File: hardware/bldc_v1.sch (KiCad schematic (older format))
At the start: 0 parts

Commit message: Updaated Driver section
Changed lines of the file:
@@
 LIBS:valves
 LIBS:infineon
+LIBS:bldc_v1-cache
 EELAYER 25 0
 EELAYER END
@@
 $EndDescr
 $Sheet
-S 1850 1450 1500 1400
+S 1800 1500 1750 1700
 U 5AAE8848
 F0 "GateDriver" 60
 F1 "GateDriver.sch" 60
+F2 "PhaseA" I L 1800 2800 60
+F3 "PhaseB" I L 1800 2900 60
+F4 "PhaseC" I L 1800 3000 60
+F5 "GND" I L 1800 3100 60
+F6 "LS_A_GATE" O R 3550 2000 60
+F7 "HS_A_GATE" O R 3550 1900 60
+F8 "LS_B_GATE" O R 3550 2200 60
+F9 "HS_B_GATE" O R 3550 2100 60
+F10 "LS_C_GATE" O R 3550 2400 60
+F11 "HS_C_GATE" O R 3550 2300 60
+F12 "LS_A_TTL_PWM" I L 1800 2150 60
+F13 "HS_A_TTL_PWM" I L 1800 2050 60
+F14 "LS_B_TTL_PWM" I L 1800 2350 60
+F15 "HS_B_TTL_PWM" I L 1800 2250 60
+F16 "LS_C_TTL_PWM" I L 1800 2550 60
+F17 "HS_C_TTL_PWM" I L 1800 2450 60
+F18 "+12V" I L 1800 1600 60
 $EndSheet
 $Sheet
-S 4950 1450 1550 1450
+S 4800 1500 1550 1450
 U 5AAE8860
 F0 "MOSFETS" 60
 F1 "MOSFETS.sch" 60
-F2 "PhaseA" O R 6500 1900 60
-F3 "+V" I L 4950 1550 60
-F4 "PhaseB" O R 6500 2050 60
-F5 "PhaseC" O R 6500 2200 60
-F6 "GND" O L 4950 2800 60
-F7 "HS_A_GATE" I L 4950 1850 60
-F8 "LS_A_GATE" I L 4950 1950 60
-F9 "HS_B_GATE" I L 4950 2050 60
-F10 "LS_B_GATE" I L 4950 2150 60
-F11 "HS_C_GATE" I L 4950 2250 60
-F12 "LS_C_GATE" I L 4950 2350 60
+F2 "PhaseA" O R 6350 1950 60
+F3 "PhaseB" O R 6350 2100 60
+F4 "PhaseC" O R 6350 2250 60
+F5 "GND" O R 6350 2800 60
+F6 "HS_A_GATE" I L 4800 1900 60
+F7 "LS_A_GATE" I L 4800 2000 60
+F8 "HS_B_GATE" I L 4800 2100 60
+F9 "LS_B_GATE" I L 4800 2200 60
+F10 "HS_C_GATE" I L 4800 2300 60
+F11 "LS_C_GATE" I L 4800 2400 60
+F12 "Vbatt" I L 4800 1600 60
 $EndSheet
+Wire Wire Line
+	3550 1900 4800 1900
+Wire Wire Line
+	3550 2000 4800 2000
+Wire Wire Line
+	3550 2100 4800 2100
+Wire Wire Line
+	3550 2200 4800 2200
+Wire Wire Line
+	3550 2300 4800 2300
+Wire Wire Line
+	3550 2400 4800 2400
+Wire Wire Line
+	6350 2800 6550 2800
+Wire Wire Line
+	6550 2800 6550 3450
+Wire Wire Line
+	6550 3450 1600 3450
+Wire Wire Line
+	1600 3450 1600 3100
+Wire Wire Line
+	1600 3100 1800 3100
+Wire Wire Line
+	6350 2250 6650 2250
+Wire Wire Line
+	6650 2250 6650 3550
+Wire Wire Line
+	6650 3550 1500 3550
+Wire Wire Line
+	1500 3550 1500 3000
+Wire Wire Line
+	1500 3000 1800 3000
+Wire Wire Line
+	6350 2100 6750 2100
+Wire Wire Line
+	6750 2100 6750 3650
+Wire Wire Line
+	6750 3650 1400 3650
+Wire Wire Line
+	1400 3650 1400 2900
+Wire Wire Line
+	1400 2900 1800 2900
+Wire Wire Line
+	6350 1950 6850 1950
+Wire Wire Line
+	6850 1950 6850 3750
+Wire Wire Line
+	6850 3750 1300 3750
+Wire Wire Line
+	1300 3750 1300 2800
+Wire Wire Line
+	1300 2800 1800 2800
 $EndSCHEMATC

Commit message: Update gate driver protection
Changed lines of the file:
@@
 LIBS:valves
 LIBS:infineon
-LIBS:bldc_v1-cache
 EELAYER 25 0
 EELAYER END
@@
 F10 "LS_C_GATE" O R 3550 2400 60
 F11 "HS_C_GATE" O R 3550 2300 60
-F12 "LS_A_TTL_PWM" I L 1800 2150 60
-F13 "HS_A_TTL_PWM" I L 1800 2050 60
-F14 "LS_B_TTL_PWM" I L 1800 2350 60
-F15 "HS_B_TTL_PWM" I L 1800 2250 60
-F16 "LS_C_TTL_PWM" I L 1800 2550 60
-F17 "HS_C_TTL_PWM" I L 1800 2450 60
+F12 "LS_A_TTL_PWM" I L 1800 2000 60
+F13 "HS_A_TTL_PWM" I L 1800 1900 60
+F14 "LS_B_TTL_PWM" I L 1800 2200 60
+F15 "HS_B_TTL_PWM" I L 1800 2100 60
+F16 "LS_C_TTL_PWM" I L 1800 2400 60
+F17 "HS_C_TTL_PWM" I L 1800 2300 60
 F18 "+12V" I L 1800 1600 60
 $EndSheet
 $Sheet
-S 4800 1500 1550 1450
+S 4800 1500 1500 1750
 U 5AAE8860
 F0 "MOSFETS" 60
 F1 "MOSFETS.sch" 60
-F2 "PhaseA" O R 6350 1950 60
-F3 "PhaseB" O R 6350 2100 60
-F4 "PhaseC" O R 6350 2250 60
-F5 "GND" O R 6350 2800 60
+F2 "PhaseA" O R 6300 1950 60
+F3 "PhaseB" O R 6300 2100 60
+F4 "PhaseC" O R 6300 2250 60
+F5 "GND" O R 6300 2800 60
 F6 "HS_A_GATE" I L 4800 1900 60
 F7 "LS_A_GATE" I L 4800 2000 60
@@
 F11 "LS_C_GATE" I L 4800 2400 60
 F12 "Vbatt" I L 4800 1600 60
+F13 "+5V" I L 4800 1700 60
+F14 "FB_A" O R 6300 1600 60
+F15 "FB_B" O R 6300 1700 60
 $EndSheet
 Wire Wire Line
@@
 	3550 2400 4800 2400
 Wire Wire Line
-	6350 2800 6550 2800
+	6300 2800 6550 2800
 Wire Wire Line
 	6550 2800 6550 3450
@@
 	1600 3100 1800 3100
 Wire Wire Line
-	6350 2250 6650 2250
+	6300 2250 6650 2250
 Wire Wire Line
 	6650 2250 6650 3550
@@
 	1500 3000 1800 3000
 Wire Wire Line
-	6350 2100 6750 2100
+	6300 2100 6750 2100
 Wire Wire Line
 	6750 2100 6750 3650
@@
 	1400 2900 1800 2900
 Wire Wire Line
-	6350 1950 6850 1950
+	6300 1950 6850 1950
 Wire Wire Line
 	6850 1950 6850 3750

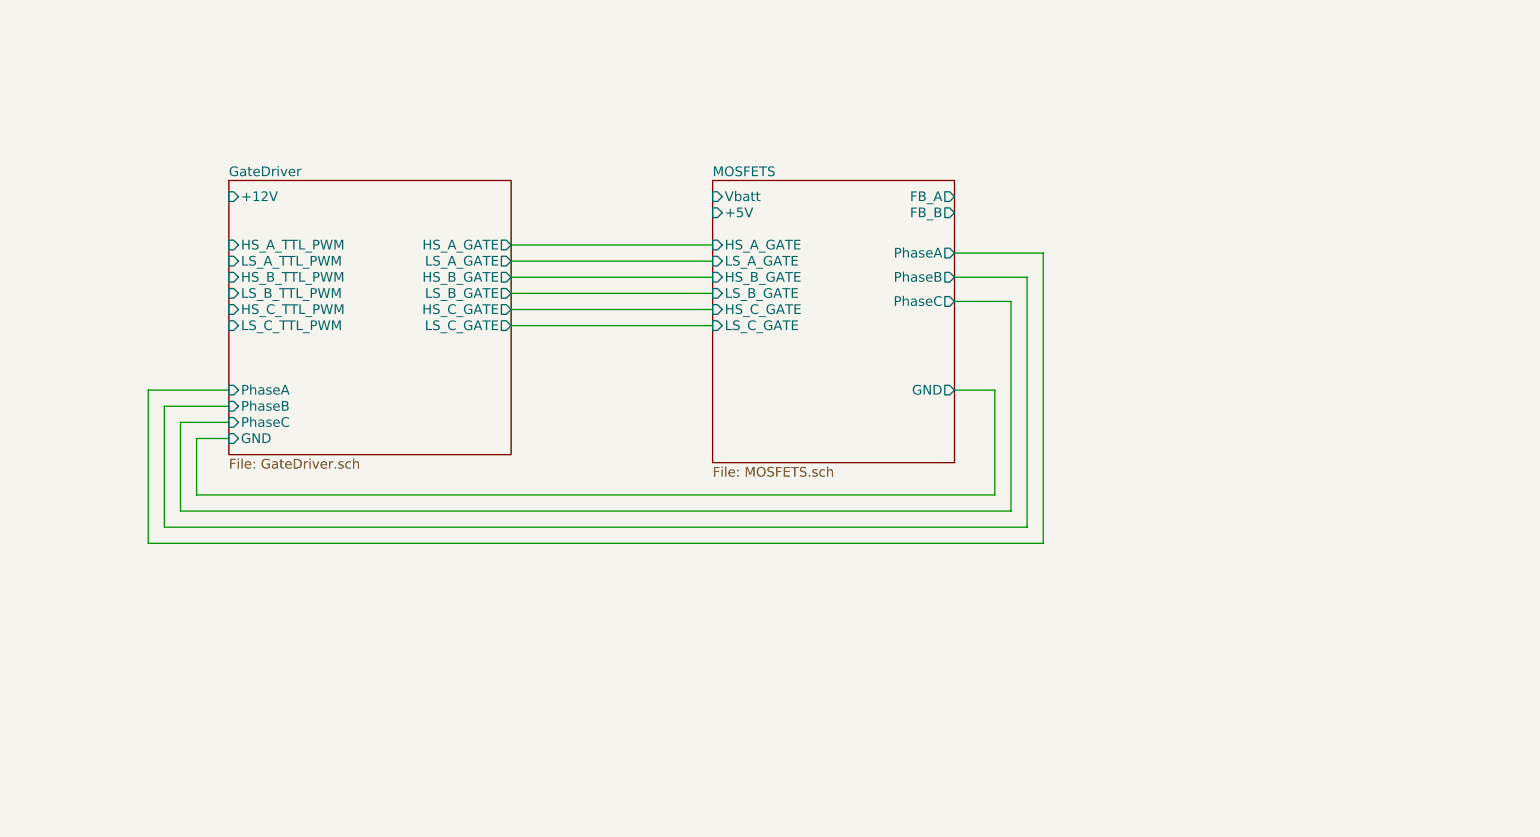
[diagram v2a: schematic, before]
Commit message: Added power converters
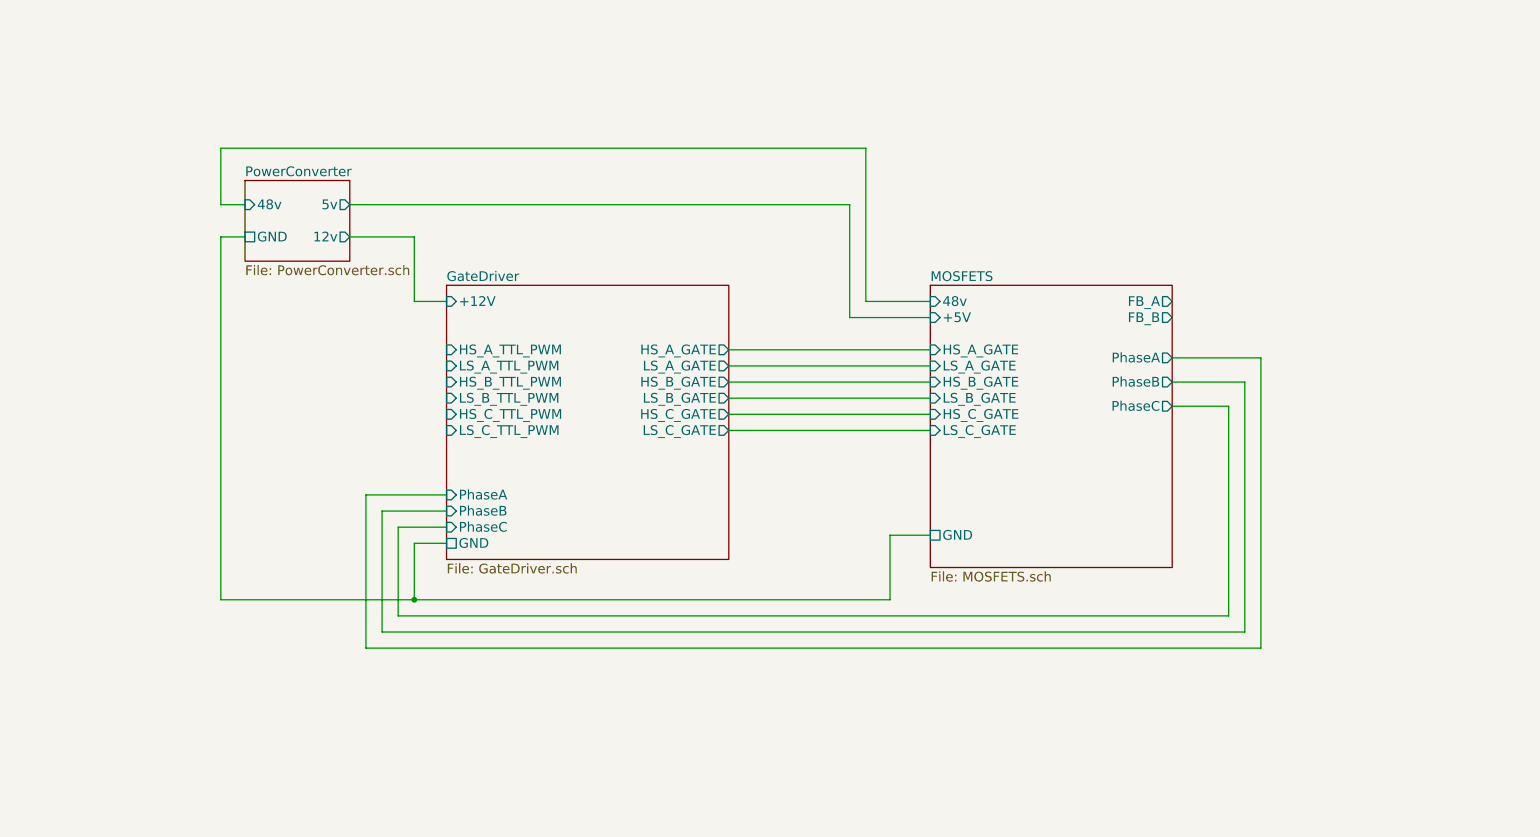
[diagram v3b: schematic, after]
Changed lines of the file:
@@
 $Descr A4 11693 8268
 encoding utf-8
-Sheet 1 3
+Sheet 1 4
 Title "Brushless DC controller"
 Date "2018-03-16"
@@
 $EndDescr
 $Sheet
-S 1800 1500 1750 1700
+S 3150 2150 1750 1700
 U 5AAE8848
 F0 "GateDriver" 60
 F1 "GateDriver.sch" 60
-F2 "PhaseA" I L 1800 2800 60
-F3 "PhaseB" I L 1800 2900 60
-F4 "PhaseC" I L 1800 3000 60
-F5 "GND" I L 1800 3100 60
-F6 "LS_A_GATE" O R 3550 2000 60
-F7 "HS_A_GATE" O R 3550 1900 60
-F8 "LS_B_GATE" O R 3550 2200 60
-F9 "HS_B_GATE" O R 3550 2100 60
-F10 "LS_C_GATE" O R 3550 2400 60
-F11 "HS_C_GATE" O R 3550 2300 60
-F12 "LS_A_TTL_PWM" I L 1800 2000 60
-F13 "HS_A_TTL_PWM" I L 1800 1900 60
-F14 "LS_B_TTL_PWM" I L 1800 2200 60
-F15 "HS_B_TTL_PWM" I L 1800 2100 60
-F16 "LS_C_TTL_PWM" I L 1800 2400 60
-F17 "HS_C_TTL_PWM" I L 1800 2300 60
-F18 "+12V" I L 1800 1600 60
+F2 "PhaseA" I L 3150 3450 60
+F3 "PhaseB" I L 3150 3550 60
+F4 "PhaseC" I L 3150 3650 60
+F5 "GND" U L 3150 3750 60
+F6 "LS_A_GATE" O R 4900 2650 60
+F7 "HS_A_GATE" O R 4900 2550 60
+F8 "LS_B_GATE" O R 4900 2850 60
+F9 "HS_B_GATE" O R 4900 2750 60
+F10 "LS_C_GATE" O R 4900 3050 60
+F11 "HS_C_GATE" O R 4900 2950 60
+F12 "LS_A_TTL_PWM" I L 3150 2650 60
+F13 "HS_A_TTL_PWM" I L 3150 2550 60
+F14 "LS_B_TTL_PWM" I L 3150 2850 60
+F15 "HS_B_TTL_PWM" I L 3150 2750 60
+F16 "LS_C_TTL_PWM" I L 3150 3050 60
+F17 "HS_C_TTL_PWM" I L 3150 2950 60
+F18 "+12V" I L 3150 2250 60
 $EndSheet
 $Sheet
-S 4800 1500 1500 1750
+S 6150 2150 1500 1750
 U 5AAE8860
 F0 "MOSFETS" 60
 F1 "MOSFETS.sch" 60
-F2 "PhaseA" O R 6300 1950 60
-F3 "PhaseB" O R 6300 2100 60
-F4 "PhaseC" O R 6300 2250 60
-F5 "GND" O R 6300 2800 60
-F6 "HS_A_GATE" I L 4800 1900 60
-F7 "LS_A_GATE" I L 4800 2000 60
-F8 "HS_B_GATE" I L 4800 2100 60
-F9 "LS_B_GATE" I L 4800 2200 60
-F10 "HS_C_GATE" I L 4800 2300 60
-F11 "LS_C_GATE" I L 4800 2400 60
-F12 "Vbatt" I L 4800 1600 60
-F13 "+5V" I L 4800 1700 60
-F14 "FB_A" O R 6300 1600 60
-F15 "FB_B" O R 6300 1700 60
+F2 "PhaseA" O R 7650 2600 60
+F3 "PhaseB" O R 7650 2750 60
+F4 "PhaseC" O R 7650 2900 60
+F5 "GND" U L 6150 3700 60
+F6 "HS_A_GATE" I L 6150 2550 60
+F7 "LS_A_GATE" I L 6150 2650 60
+F8 "HS_B_GATE" I L 6150 2750 60
+F9 "LS_B_GATE" I L 6150 2850 60
+F10 "HS_C_GATE" I L 6150 2950 60
+F11 "LS_C_GATE" I L 6150 3050 60
+F12 "+5V" I L 6150 2350 60
+F13 "FB_A" O R 7650 2250 60
+F14 "FB_B" O R 7650 2350 60
+F15 "48v" I L 6150 2250 60
 $EndSheet
 Wire Wire Line
-	3550 1900 4800 1900
+	4900 2550 6150 2550
 Wire Wire Line
-	3550 2000 4800 2000
+	4900 2650 6150 2650
 Wire Wire Line
-	3550 2100 4800 2100
+	4900 2750 6150 2750
 Wire Wire Line
-	3550 2200 4800 2200
+	4900 2850 6150 2850
 Wire Wire Line
-	3550 2300 4800 2300
+	4900 2950 6150 2950
 Wire Wire Line
-	3550 2400 4800 2400
+	4900 3050 6150 3050
 Wire Wire Line
-	6300 2800 6550 2800
+	2950 4100 2950 3750
 Wire Wire Line
-	6550 2800 6550 3450
+	2950 3750 3150 3750
 Wire Wire Line
-	6550 3450 1600 3450
+	7650 2900 8000 2900
 Wire Wire Line
-	1600 3450 1600 3100
+	8000 2900 8000 4200
 Wire Wire Line
-	1600 3100 1800 3100
+	8000 4200 2850 4200
 Wire Wire Line
-	6300 2250 6650 2250
+	2850 4200 2850 3650
 Wire Wire Line
-	6650 2250 6650 3550
+	2850 3650 3150 3650
 Wire Wire Line
-	6650 3550 1500 3550
+	7650 2750 8100 2750
 Wire Wire Line
-	1500 3550 1500 3000
+	8100 2750 8100 4300
 Wire Wire Line
-	1500 3000 1800 3000
+	8100 4300 2750 4300
 Wire Wire Line
-	6300 2100 6750 2100
+	2750 4300 2750 3550
 Wire Wire Line
-	6750 2100 6750 3650
+	2750 3550 3150 3550
 Wire Wire Line
-	6750 3650 1400 3650
+	7650 2600 8200 2600
 Wire Wire Line
-	1400 3650 1400 2900
+	8200 2600 8200 4400
 Wire Wire Line
-	1400 2900 1800 2900
+	8200 4400 2650 4400
 Wire Wire Line
-	6300 1950 6850 1950
+	2650 4400 2650 3450
 Wire Wire Line
-	6850 1950 6850 3750
+	2650 3450 3150 3450
+$Sheet
+S 1900 1500 650  500
+U 5AB4694D
+F0 "PowerConverter" 60
+F1 "PowerConverter.sch" 60
+F2 "GND" U L 1900 1850 60
+F3 "12v" O R 2550 1850 60
+F4 "48v" I L 1900 1650 60
+F5 "5v" O R 2550 1650 60
+$EndSheet
 Wire Wire Line
-	6850 3750 1300 3750
+	2550 1650 5650 1650
 Wire Wire Line
-	1300 3750 1300 2800
+	5650 1650 5650 2350
 Wire Wire Line
-	1300 2800 1800 2800
+	5650 2350 6150 2350
+Wire Wire Line
+	3150 2250 2950 2250
+Wire Wire Line
+	2950 2250 2950 1850
+Wire Wire Line
+	2950 1850 2550 1850
+Wire Wire Line
+	6150 3700 5900 3700
+Wire Wire Line
+	5900 4100 5900 3700
+Wire Wire Line
+	1750 4100 2950 4100
+Wire Wire Line
+	2950 4100 5900 4100
+Wire Wire Line
+	1750 4100 1750 1850
+Wire Wire Line
+	1750 1850 1900 1850
+Connection ~ 2950 4100
+Wire Wire Line
+	6150 2250 5750 2250
+Wire Wire Line
+	5750 2250 5750 1300
+Wire Wire Line
+	5750 1300 1750 1300
+Wire Wire Line
+	1750 1300 1750 1650
+Wire Wire Line
+	1750 1650 1900 1650
 $EndSCHEMATC

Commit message: added microcontroller page
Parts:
- added J1, J2: Screw_Terminal_01x02, symbol Screw_Terminal_01x02
- added J3: Screw_Terminal_01x03, symbol Screw_Terminal_01x03
- added J4: Conn_01x06, symbol Conn_01x06
- added J5: Screw_Terminal_01x05, symbol Screw_Terminal_01x05
- added R1: 10k, symbol R
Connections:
- net labels added: 48v, 5v, FB_A, FB_B, GND
- wire segments 40 -> 58
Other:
- note added: "Intentionally connected \nbackwards"

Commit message: cleaned up schematic
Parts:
- J4: PN (none) -> TSM-106-01-L-SV
- J5: PN (none) -> 1935190
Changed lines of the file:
@@
 LIBS:crf_1
 LIBS:STM32F4-DISCOVERY-SIMON
-LIBS:bldc_v1-cache
 EELAYER 25 0
 EELAYER END
@@
 P 1050 3500
 F 0 "J4" H 1050 3800 50  0000 C CNN
-F 1 "Conn_01x06" H 1050 3100 50  0000 C CNN
+F 1 "Conn_01x06" V 1150 3500 50  0000 C CNN
 F 2 "" H 1050 3500 50  0001 C CNN
 F 3 "" H 1050 3500 50  0001 C CNN
+F 4 "TSM-106-01-L-SV" V 1250 3500 60  0000 C CNN "PN"
 	1    1050 3500
 	-1   0    0    1
@@
 U 1 1 5AB91720
 P 1900 2300
-F 0 "J5" V 2050 2300 50  0000 C CNN
+F 0 "J5" V 2200 2300 50  0000 C CNN
 F 1 "Screw_Terminal_01x05" V 2000 2300 50  0000 C CNN
 F 2 "" H 1900 2300 50  0001 C CNN
 F 3 "" H 1900 2300 50  0001 C CNN
+F 4 "1935190" V 2100 2300 60  0000 C CNN "PN"
 	1    1900 2300
 	0    -1   -1   0

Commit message: associated footprints
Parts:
- J1: footprint (none) -> Connectors_Terminal_Blocks:TerminalBlock_bornier-2_P5.08mm
- J4: footprint (none) -> Pin_Headers:Pin_Header_Straight_1x06_Pitch2.54mm_SMD_Pin1Right
- J5: footprint (none) -> Connectors_Terminal_Blocks:TerminalBlock_bornier-5_P5.08mm
- R1: footprint (none) -> Resistors_SMD:R_0201
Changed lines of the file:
@@
 F 0 "J1" H 4150 4700 50  0000 C CNN
 F 1 "Screw_Terminal_01x02" V 4250 4600 50  0000 C CNN
-F 2 "" H 4150 4600 50  0001 C CNN
+F 2 "Connectors_Terminal_Blocks:TerminalBlock_bornier-2_P5.08mm" H 4150 4600 50  0001 C CNN
 F 3 "" H 4150 4600 50  0001 C CNN
 F 4 "1935161 " V 4350 4600 60  0000 C CNN "PN"
@@
 F 0 "R1" V 3730 4350 50  0000 C CNN
 F 1 "10k" V 3650 4350 50  0000 C CNN
-F 2 "" V 3580 4350 50  0001 C CNN
+F 2 "Resistors_SMD:R_0201" V 3580 4350 50  0001 C CNN
 F 3 "" H 3650 4350 50  0001 C CNN
 F 4 "RC0201JR-0710KL" V 3550 4300 60  0000 C CNN "PN"
@@
 F 0 "J4" H 1050 3800 50  0000 C CNN
 F 1 "Conn_01x06" V 1150 3500 50  0000 C CNN
-F 2 "" H 1050 3500 50  0001 C CNN
+F 2 "Pin_Headers:Pin_Header_Straight_1x06_Pitch2.54mm_SMD_Pin1Right" H 1050 3500 50  0001 C CNN
 F 3 "" H 1050 3500 50  0001 C CNN
 F 4 "TSM-106-01-L-SV" V 1250 3500 60  0000 C CNN "PN"
@@
 F 0 "J5" V 2200 2300 50  0000 C CNN
 F 1 "Screw_Terminal_01x05" V 2000 2300 50  0000 C CNN
-F 2 "" H 1900 2300 50  0001 C CNN
+F 2 "Connectors_Terminal_Blocks:TerminalBlock_bornier-5_P5.08mm" H 1900 2300 50  0001 C CNN
 F 3 "" H 1900 2300 50  0001 C CNN
 F 4 "1935190" V 2100 2300 60  0000 C CNN "PN"

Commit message: annotated schematic
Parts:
- renumbered J4 to J1, J5 to J3, J1 to J4, J3 to J5
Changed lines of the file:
@@
 	1400 3200 1250 3200
 $Comp
-L Screw_Terminal_01x02 J1
+L Screw_Terminal_01x02 J4
 U 1 1 5AB7FC0B
 P 4150 4600
-F 0 "J1" H 4150 4700 50  0000 C CNN
+F 0 "J4" H 4150 4700 50  0000 C CNN
 F 1 "Screw_Terminal_01x02" V 4250 4600 50  0000 C CNN
 F 2 "Connectors_Terminal_Blocks:TerminalBlock_bornier-2_P5.08mm" H 4150 4600 50  0001 C CNN
@@
 	1650 1050 1400 1050
 $Comp
-L Screw_Terminal_01x03 J3
+L Screw_Terminal_01x03 J5
 U 1 1 5AB8C60E
 P 7350 4750
-F 0 "J3" H 7350 4950 50  0000 C CNN
+F 0 "J5" H 7350 4950 50  0000 C CNN
 F 1 "Screw_Terminal_01x03" V 7450 4750 50  0000 C CNN
 F 2 "" H 7350 4750 50  0001 C CNN
@@
 Connection ~ 7250 3750
 $Comp
-L Conn_01x06 J4
+L Conn_01x06 J1
 U 1 1 5AB8F4C0
 P 1050 3500
-F 0 "J4" H 1050 3800 50  0000 C CNN
+F 0 "J1" H 1050 3800 50  0000 C CNN
 F 1 "Conn_01x06" V 1150 3500 50  0000 C CNN
 F 2 "Pin_Headers:Pin_Header_Straight_1x06_Pitch2.54mm_SMD_Pin1Right" H 1050 3500 50  0001 C CNN
@@
 $EndComp
 $Comp
-L Screw_Terminal_01x05 J5
+L Screw_Terminal_01x05 J3
 U 1 1 5AB91720
 P 1900 2300
-F 0 "J5" V 2200 2300 50  0000 C CNN
+F 0 "J3" V 2200 2300 50  0000 C CNN
 F 1 "Screw_Terminal_01x05" V 2000 2300 50  0000 C CNN
 F 2 "Connectors_Terminal_Blocks:TerminalBlock_bornier-5_P5.08mm" H 1900 2300 50  0001 C CNN

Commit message: created new footprints, modified schematic
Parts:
- removed J2: Screw_Terminal_01x02, symbol Screw_Terminal_01x02
- removed J4: Screw_Terminal_01x02, Connectors_Terminal_Blocks:TerminalBlock_bornier-2_P5.08mm, symbol Screw_Terminal_01x02
- removed R1: 10k, Resistors_SMD:R_0201, symbol R
- added J2: 1x2_ScrewTerminal_65A, custom:1x2_ScrewTerminal_65A, symbol 1x2_ScrewTerminal_65A
- added J4: RJ45, Connectors:RJ45_8, symbol RJ45
- J3: footprint Connectors_Terminal_Blocks:TerminalBlock_bornier-5_P5.08mm -> custom:1x5_ScrewTerminal_1A
- J5: footprint (none) -> custom:1x3_ScrewTerminal_65A
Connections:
- wire segments 58 -> 59
- no-connect marks 0 -> 8
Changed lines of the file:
@@
 F15 "FB_A" I L 2600 3800 60
 F16 "FB_B" I L 2600 3900 60
-F17 "Throttle" I R 3900 3950 60
+F17 "I2C_SCL" U R 3900 3750 60
+F18 "I2C_SDA" U R 3900 3850 60
 $EndSheet
 Wire Wire Line
@@
 Wire Wire Line
 	1400 3200 1250 3200
-$Comp
-L Screw_Terminal_01x02 J4
-U 1 1 5AB7FC0B
-P 4150 4600
-F 0 "J4" H 4150 4700 50  0000 C CNN
-F 1 "Screw_Terminal_01x02" V 4250 4600 50  0000 C CNN
-F 2 "Connectors_Terminal_Blocks:TerminalBlock_bornier-2_P5.08mm" H 4150 4600 50  0001 C CNN
-F 3 "" H 4150 4600 50  0001 C CNN
-F 4 "1935161 " V 4350 4600 60  0000 C CNN "PN"
-	1    4150 4600
-	0    1    1    0
-$EndComp
-Text Label 4150 4200 0    60   ~ 0
-5v
-Wire Wire Line
-	4150 4200 4150 4400
-Wire Wire Line
-	3900 3950 4050 3950
-Wire Wire Line
-	4050 3950 4050 4400
-$Comp
-L R R1
-U 1 1 5AB81ECB
-P 3650 4350
-F 0 "R1" V 3730 4350 50  0000 C CNN
-F 1 "10k" V 3650 4350 50  0000 C CNN
-F 2 "Resistors_SMD:R_0201" V 3580 4350 50  0001 C CNN
-F 3 "" H 3650 4350 50  0001 C CNN
-F 4 "RC0201JR-0710KL" V 3550 4300 60  0000 C CNN "PN"
-	1    3650 4350
-	0    1    1    0
-$EndComp
-Wire Wire Line
-	3800 4350 4050 4350
-Connection ~ 4050 4350
-Text Label 3100 4350 2    60   ~ 0
-GND
-Wire Wire Line
-	3100 4350 3500 4350
+Text Label 4500 4200 1    60   ~ 0
+5v
+Wire Wire Line
+	4500 4200 4500 4450
+Text Label 4200 4200 1    60   ~ 0
+GND
 Text Label 3350 1750 2    60   ~ 0
 48v
 Connection ~ 3500 1750
-$Comp
-L Screw_Terminal_01x02 J2
-U 1 1 5AB887E8
-P 1200 1050
-F 0 "J2" H 1200 1150 50  0000 C CNN
-F 1 "Screw_Terminal_01x02" H 1200 1200 50  0000 C CNN
-F 2 "" H 1200 1050 50  0001 C CNN
-F 3 "" H 1200 1050 50  0001 C CNN
-F 4 "1986660-2" H 1200 850 60  0000 C CNN "PN"
-	1    1200 1050
-	-1   0    0    1
-$EndComp
 Text Label 1650 950  0    60   ~ 0
 48v
@@
 Wire Wire Line
 	1650 1050 1400 1050
-$Comp
-L Screw_Terminal_01x03 J5
-U 1 1 5AB8C60E
-P 7350 4750
-F 0 "J5" H 7350 4950 50  0000 C CNN
-F 1 "Screw_Terminal_01x03" V 7450 4750 50  0000 C CNN
-F 2 "" H 7350 4750 50  0001 C CNN
-F 3 "" H 7350 4750 50  0001 C CNN
-F 4 "1986660-3" V 7550 4750 60  0000 C CNN "PN"
-	1    7350 4750
-	0    1    1    0
-$EndComp
 Wire Wire Line
 	7450 4550 7450 3950
@@
 F 0 "J3" V 2200 2300 50  0000 C CNN
 F 1 "Screw_Terminal_01x05" V 2000 2300 50  0000 C CNN
-F 2 "Connectors_Terminal_Blocks:TerminalBlock_bornier-5_P5.08mm" H 1900 2300 50  0001 C CNN
+F 2 "custom:1x5_ScrewTerminal_1A" H 1900 2300 50  0001 C CNN
 F 3 "" H 1900 2300 50  0001 C CNN
 F 4 "1935190" V 2100 2300 60  0000 C CNN "PN"
@@
 Wire Wire Line
 	2000 2600 2000 2500
+$Comp
+L 1x2_ScrewTerminal_65A J2
+U 1 1 5ABA8578
+P 1200 1050
+F 0 "J2" H 1200 1150 50  0000 C CNN
+F 1 "1x2_ScrewTerminal_65A" H 1200 850 50  0000 C CNN
+F 2 "custom:1x2_ScrewTerminal_65A" H 1200 1050 50  0001 C CNN
+F 3 "" H 1200 1050 50  0001 C CNN
+	1    1200 1050
+	-1   0    0    1
+$EndComp
+$Comp
+L Screw_Terminal_01x03 J5
+U 1 1 5ABABEF7
+P 7350 4750
+F 0 "J5" H 7350 4950 50  0000 C CNN
+F 1 "Screw_Terminal_01x03" V 7450 4750 50  0000 C CNN
+F 2 "custom:1x3_ScrewTerminal_65A" H 7350 4750 50  0001 C CNN
+F 3 "" H 7350 4750 50  0001 C CNN
+F 4 "1986660-3" V 7550 4750 60  0000 C CNN "PN"
+	1    7350 4750
+	0    1    1    0
+$EndComp
+$Comp
+L RJ45 J4
+U 1 1 5ABC4D57
+P 4350 4900
+F 0 "J4" H 4550 5400 50  0000 C CNN
+F 1 "RJ45" H 4200 5400 50  0000 C CNN
+F 2 "Connectors:RJ45_8" H 4350 4900 50  0001 C CNN
+F 3 "" H 4350 4900 50  0001 C CNN
+F 4 "SS-6488S-A-NF" H 4350 5500 60  0000 C CNN "PN"
+	1    4350 4900
+	-1   0    0    1
+$EndComp
+Wire Wire Line
+	4200 4200 4200 4450
+Wire Wire Line
+	3900 3750 4100 3750
+Wire Wire Line
+	4100 3750 4100 4450
+Wire Wire Line
+	4000 4450 4000 3850
+Wire Wire Line
+	4000 3850 3900 3850
+NoConn ~ 3800 5250
+NoConn ~ 1250 3300
+NoConn ~ 1250 3400
+NoConn ~ 1250 3700
+NoConn ~ 4700 4450
+NoConn ~ 4600 4450
+NoConn ~ 4400 4450
+NoConn ~ 4300 4450
 $EndSCHEMATC
